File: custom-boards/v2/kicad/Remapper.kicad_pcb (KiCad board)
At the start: 2 copper layers, 25 x 25 mm, 49 parts, among them J1 Conn_01x06, J101 Conn_01x06, U103 RP2040, U105 W25Q128JVS, U3 RP2040, U4 TLV73333PDBV, U5 W25Q128JVS, Y1 Crystal_GND24, Y101 Crystal_GND24

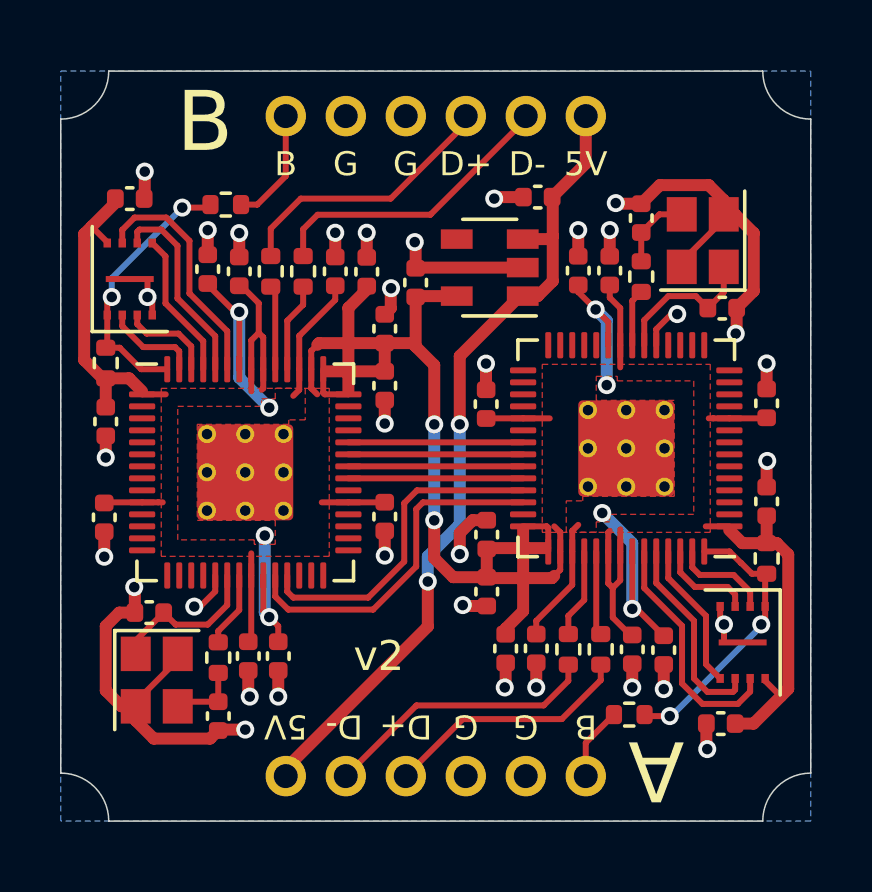
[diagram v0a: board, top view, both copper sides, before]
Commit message: Update custom boards
This commit makes the following changes to the custom PCB designs.

v1-v5: flash chip footprint changed, previous one caused issues in
manufacturing. Some other components moved around as a result.

v1-v5: flash chip changed from 1 megabyte to 2 megabyte one.

v1: USB Type A port component changed, previous one was consistently
soldered on crooked by JLCPCB.

The new designs are named v1.1-v5.1.

Schematics and enclosure files are unchanged.
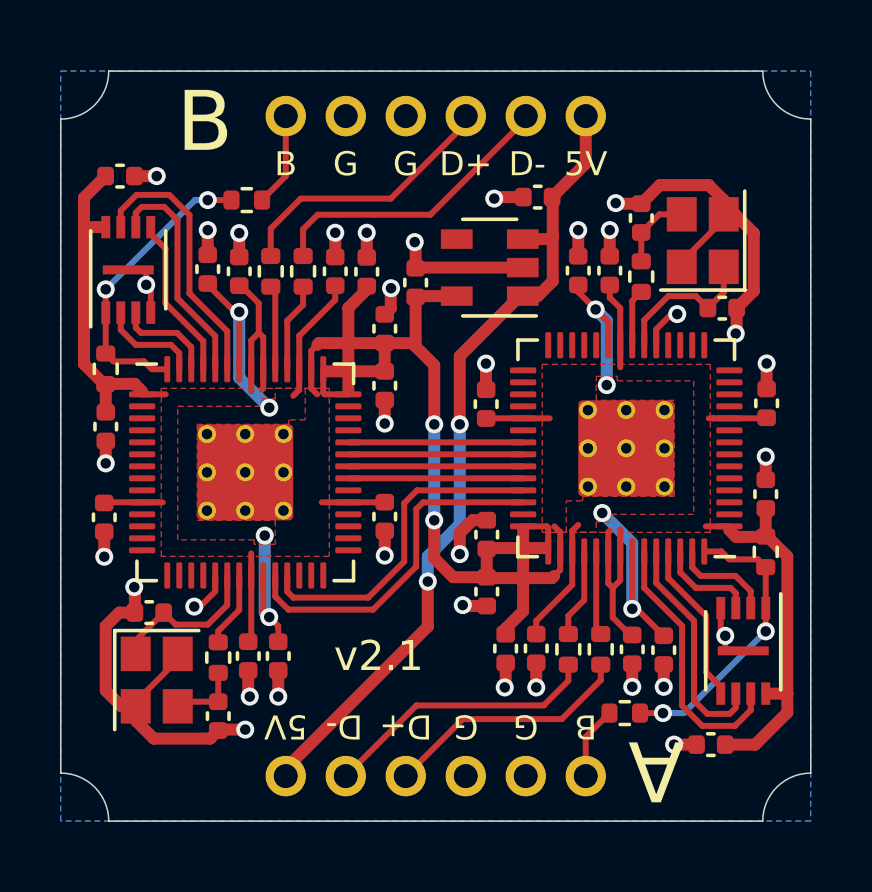
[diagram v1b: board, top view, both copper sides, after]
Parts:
- U4: footprint Package_TO_SOT_SMD:SOT-23-5 -> SOT:SOT-23-5
- moved C17 0.82 mm to (131.5, 38.5)
- moved C117 0.77 mm to (151.2, 57.5)
- moved R6 0.72 mm to (135.7, 39.3)
- moved U5 0.31 mm to (131.8, 41.6)
- moved U105 0.28 mm to (152.2, 54.3)
- moved C104 0.25 mm to (153.0, 49.1)
- moved R105 0.22 mm to (153.0, 51.0)
- moved R5 0.19 mm to (131.0, 44.9)
- moved C4 0.17 mm to (131.0, 46.9)
- moved R106 0.16 mm to (148.3, 56.4)
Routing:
- net +3V3: track 86.3 -> 87.7 mm
- net QSPI_SD3: track 7.97 -> 9.00 mm
- net QSPI_SCLK: track 6.61 -> 7.62 mm
- net 1QSPI_SD3: track 8.08 -> 9.00 mm
- net 1QSPI_SCLK: track 6.72 -> 7.62 mm
- net QSPI_SS: track 9.06 -> 9.83 mm
- net BOOTSEL: track 3.88 -> 3.13 mm
- net QSPI_SD0: track 4.91 -> 5.46 mm
- net 1QSPI_SD0: track 4.95 -> 5.46 mm
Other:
- board text added: "v2.1"
- board text removed: "v2"
